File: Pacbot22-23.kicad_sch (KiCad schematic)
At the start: 8 parts, among them SW1 SW_Push, U1 ATmega32U4-A, Y1 16Mhz

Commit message: Finished backup of schematic
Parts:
- added C20, C21, C22, C23, C24, C25: 0.1uF, symbol Device:C_Small
- added C26: 10uF, symbol Device:C_Small
- added J1, J2, J3, J4, J5, J6, J7, J8: VL6180X, symbol CustomSymbols:VL6180X
- added J10: Screw_Terminal_01x02, symbol Connector:Screw_Terminal_01x02
- added J20: USB_B_Micro, symbol Connector:USB_B_Micro
- added J30: BNO-055, symbol CustomSymbols:BNO-055
- added J40, J41: 6V_DC_Motor, symbol CustomSymbols:6V_DC_Motor
- added R1, R2: 22r, symbol Device:R_Small
- added U10: SN74HCS264DR, SOIC127P600X175-14N, symbol CustomSymbols:SN74HCS264DR
- added U? (x2): L9110_HBridge, symbol CustomSymbols:L9110_HBridge
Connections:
- net +5V: now also C20.1, C21.1, C22.1, C23.1, C24.1, C25.1, C26.1, J1.1 (VIN), J10.1 (Pin_1), J2.1 (VIN), J20.1 (VBUS), J3.1 (VIN), J30.1 (VIN), J4.1 (VIN), J40.4 (E_PWR), J41.4 (E_PWR), J5.1 (VIN), J6.1 (VIN), J7.1 (VIN), J8.1 (VIN), U10.1 (A), U10.14 (VCC), U10.9 (~{CLR}), U?.2 (VCC), U?.2 (VCC), U?.3 (VCC), U?.3 (VCC)
- net BNO_INT: now also J30.7 (INT)
- net BNO_RST: now also J30.6 (RST)
- net D+: now also R1.2
- net D-: now also R2.2
- net ENC11: now also J40.5 (ENCA)
- net ENC12: now also J40.6 (ENCB)
- net ENC21: now also J41.5 (ENCA)
- net ENC22: now also J41.6 (ENCB)
- net GND: now also C20.2, C21.2, C22.2, C23.2, C24.2, C25.2, C26.2, J1.2 (GND), J10.2 (Pin_2), J2.2 (GND), J20.5 (GND), J3.2 (GND), J30.3 (GND), J30.8 (ADR), J4.2 (GND), J40.3 (E_GND), J41.3 (E_GND), J5.2 (GND), J6.2 (GND), J7.2 (GND), J8.2 (GND), U10.7 (GND), U?.5 (GND), U?.5 (GND), U?.8 (GND), U?.8 (GND)
- net M11: now also U?.6 (IA)
- net M12: now also U?.7 (IB)
- net M21: now also U?.6 (IA)
- net M22: now also U?.7 (IB)
- net SCL: now also J1.3 (SCL), J2.3 (SCL), J3.3 (SCL), J30.4 (SCL), J4.3 (SCL), J5.3 (SCL), J6.3 (SCL), J7.3 (SCL), J8.3 (SCL)
- net SDA: now also J1.4 (SDA), J2.4 (SDA), J3.4 (SDA), J30.5 (SDA), J4.4 (SDA), J5.4 (SDA), J6.4 (SDA), J7.4 (SDA), J8.4 (SDA)
- net SR_C: now also U10.8 (CLK)
- net SR_D: now also U10.2 (B)
- new net: J20.3 (D+), R1.1
- new net: J20.2 (D-), R2.1
- new net M1_PWR+: J40.1 (M_PWR+), U?.1 (OA)
- new net M1_PWR-: J40.2 (M_PWR-), U?.4 (OB)
- new net M2_PWR+: J41.1 (M_PWR+), U?.1 (OA)
- new net M2_PWR-: J41.2 (M_PWR-), U?.4 (OB)
- new net XS1: J1.6 (XSHUT), U10.3 (QA)
- new net XS2: J2.6 (XSHUT), U10.4 (QB)
- new net XS3: J3.6 (XSHUT), U10.5 (QC)
- new net XS4: J4.6 (XSHUT), U10.6 (QD)
- new net XS5: J5.6 (XSHUT), U10.10 (QE)
- new net XS6: J6.6 (XSHUT), U10.11 (QF)
- new net XS7: J7.6 (XSHUT), U10.12 (QG)
- new net XS8: J8.6 (XSHUT), U10.13 (QH)
- no-connect marks 0 -> 13

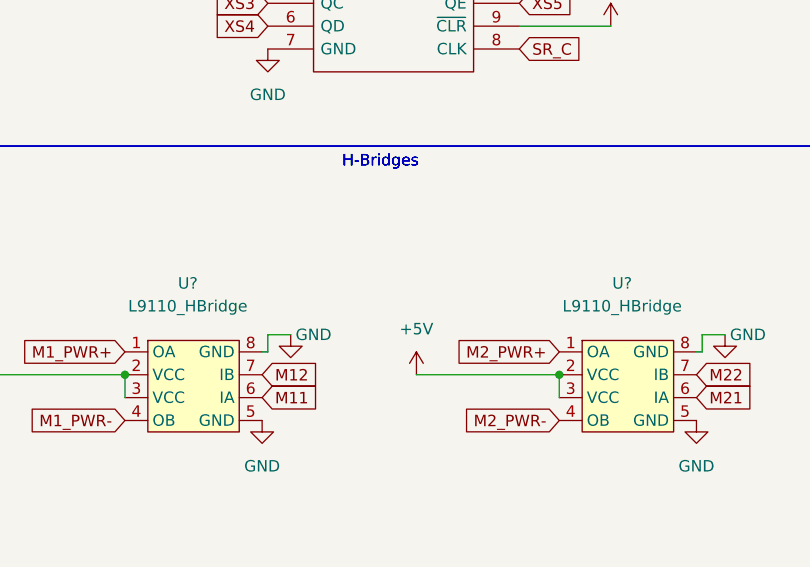
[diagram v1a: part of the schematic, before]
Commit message: Fixed question mark issue
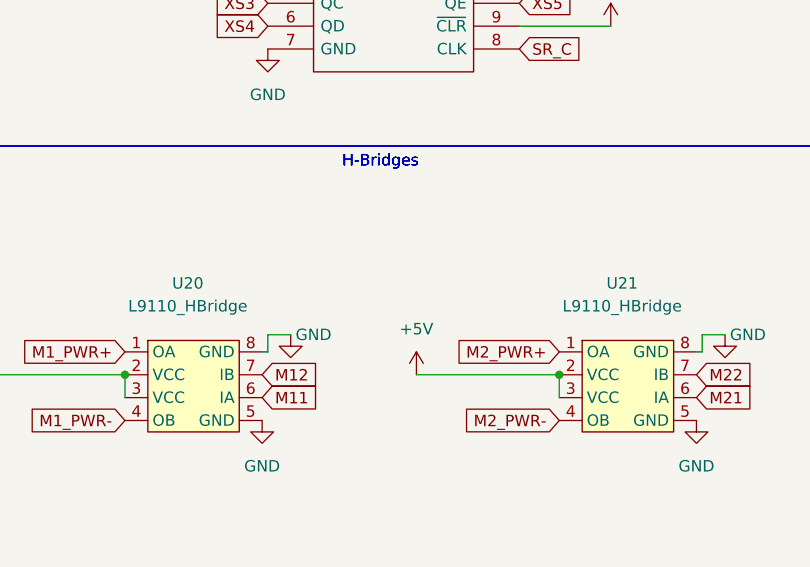
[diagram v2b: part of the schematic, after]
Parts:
- gave numbers to parts that had none: 2
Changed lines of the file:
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@@
   (symbol (lib_id "CustomSymbols:L9110_HBridge") (at 259.08 139.7 0) (unit 1)
     (in_bom yes) (on_board yes) (fields_autoplaced)
-    (property "Reference" "U?" (id 0) (at 258.445 128.27 0))
+    (property "Reference" "U21" (id 0) (at 258.445 128.27 0))
     (property "Value" "L9110_HBridge" (id 1) (at 258.445 130.81 0))
     (property "Footprint" "" (id 2) (at 259.08 139.7 0)
@@
   (symbol (lib_id "CustomSymbols:L9110_HBridge") (at 210.82 139.7 0) (unit 1)
     (in_bom yes) (on_board yes) (fields_autoplaced)
-    (property "Reference" "U?" (id 0) (at 210.185 128.27 0))
+    (property "Reference" "U20" (id 0) (at 210.185 128.27 0))
     (property "Value" "L9110_HBridge" (id 1) (at 210.185 130.81 0))
     (property "Footprint" "" (id 2) (at 210.82 139.7 0)
@@
       (reference "U10") (unit 1) (value "SN74HCS264DR") (footprint "SOIC127P600X175-14N")
     )
+    (path "/99bff380-bb67-4944-bd8d-cd24f3744ecf"
+      (reference "U20") (unit 1) (value "L9110_HBridge") (footprint "")
+    )
     (path "/0ffed388-a01b-4ab0-a4ac-63b7eb56caa1"
-      (reference "U?") (unit 1) (value "L9110_HBridge") (footprint "")
-    )
-    (path "/99bff380-bb67-4944-bd8d-cd24f3744ecf"
-      (reference "U?") (unit 1) (value "L9110_HBridge") (footprint "")
+      (reference "U21") (unit 1) (value "L9110_HBridge") (footprint "")
     )
     (path "/e4a0ec35-7592-44cc-8cca-728fc52023c0"
